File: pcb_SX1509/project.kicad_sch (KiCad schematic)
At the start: 43 parts, among them IC1 SX1509QBIULTRT

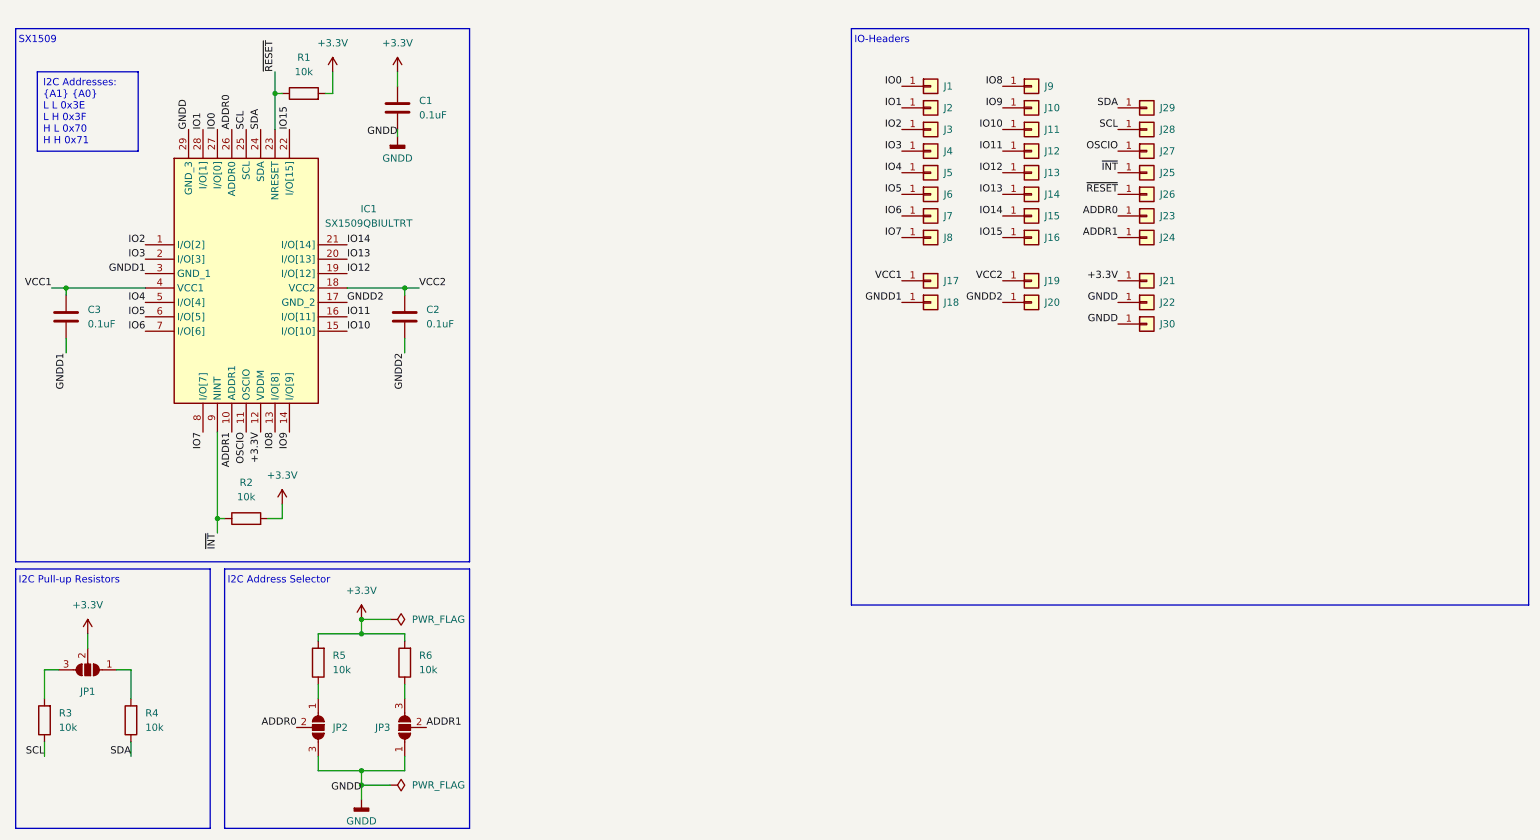
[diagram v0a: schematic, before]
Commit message: Standard output pin design for SX1509 PCB and add a new variant based on PCA9685
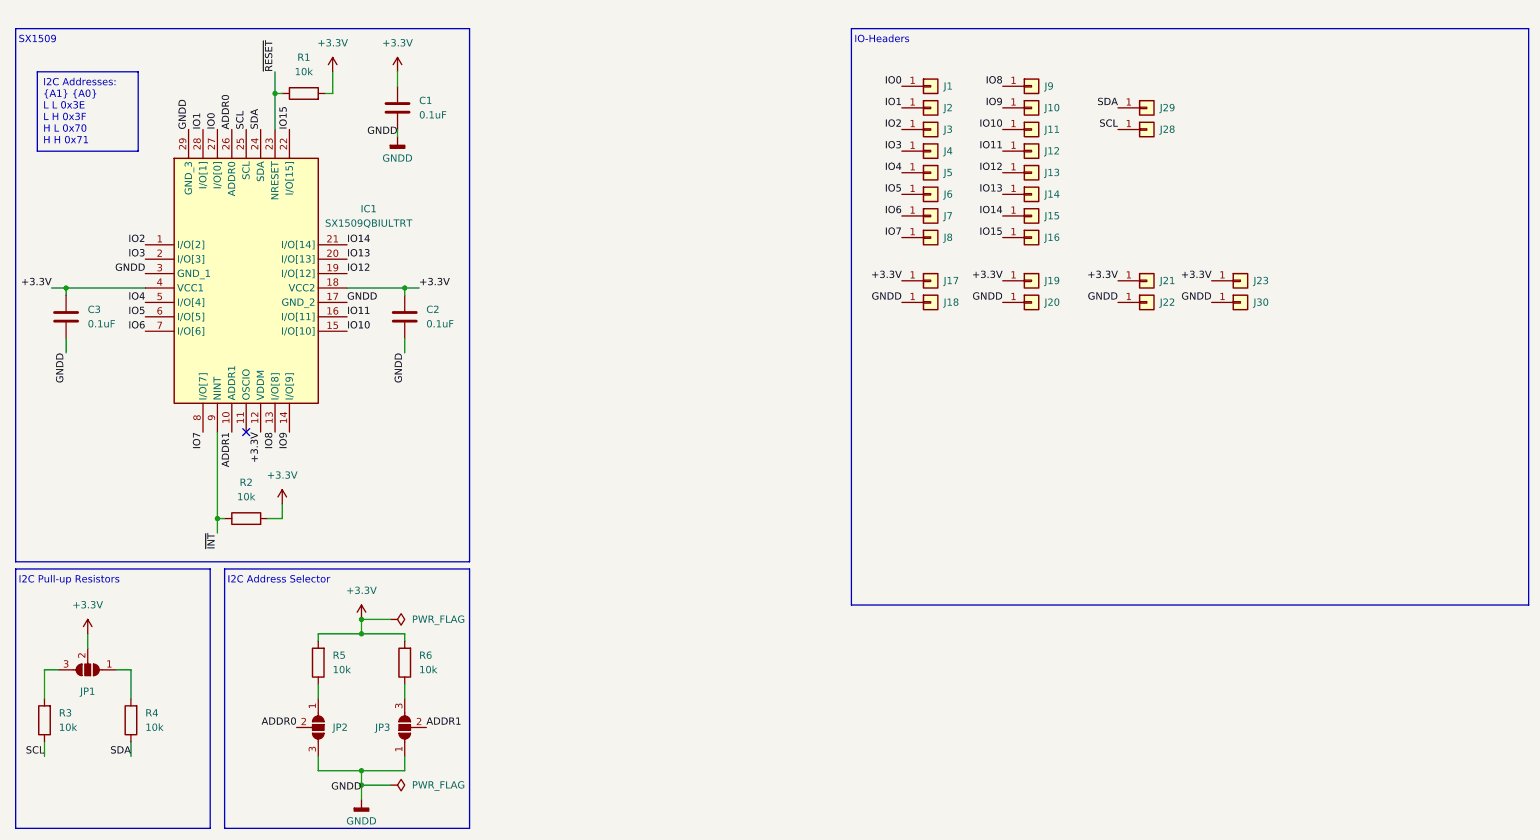
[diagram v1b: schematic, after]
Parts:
- removed J24, J25, J26, J27: ~, Castellated_Holes:Castellated_Hole02, symbol Connector_Generic:Conn_01x01
- JP1, JP2, JP3: footprint Jumper:SolderJumper-3_P1.3mm_Open_RoundedPad1.0x1.5mm -> Jumper:SolderJumper-3_P1.3mm_Open_RoundedPad1.0x1.5mm
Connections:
- net GNDD1 is gone; now on net GNDD: C3.2, IC1.3 (GND_1), J18.1 (Pin_1)
- net GNDD2 is gone; now on net GNDD: C2.2, IC1.17 (GND_2), J20.1 (Pin_1)
- net VCC1 is gone; now on net +3.3V: C3.1, IC1.4 (VCC1), J17.1 (Pin_1)
- net VCC2 is gone; now on net +3.3V: C2.1, IC1.18 (VCC2), J19.1 (Pin_1)
- net +3.3V: now also J23.1 (Pin_1)
- net ADDR0: no longer J23.1 (Pin_1)
- net OSCIO: no longer names the net of IC1.11 (OSCIO)
- no-connect marks 0 -> 1
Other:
- moved on the sheet: J30

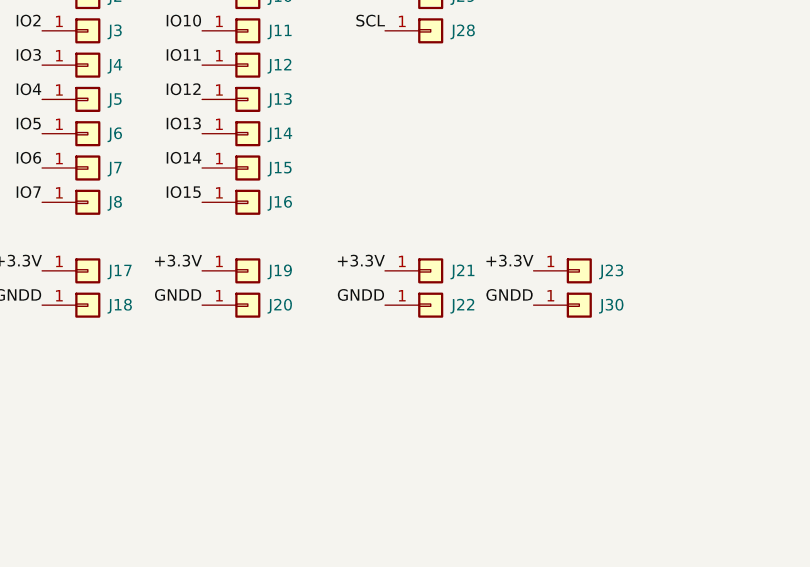
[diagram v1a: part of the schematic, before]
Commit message: Remove connector on own side
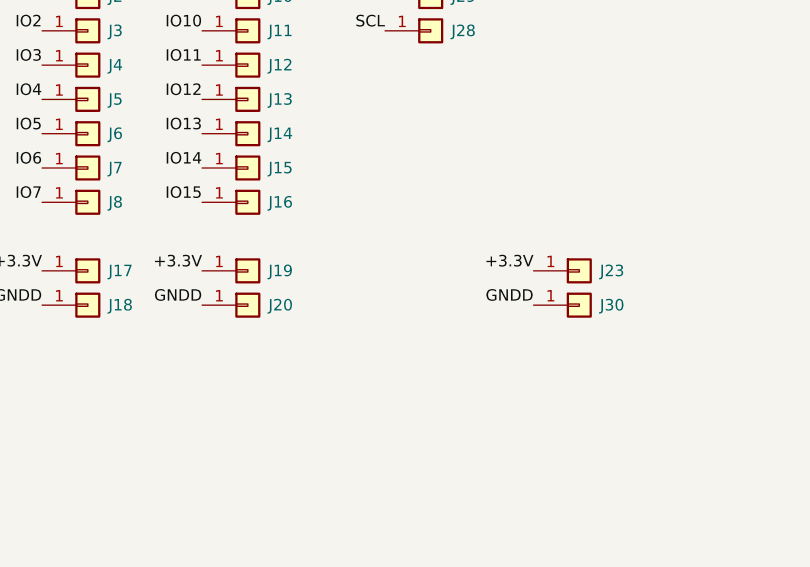
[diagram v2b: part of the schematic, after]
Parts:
- removed J21, J22: ~, Castellated_Holes:Castellated_Hole02, symbol Connector_Generic:Conn_01x01
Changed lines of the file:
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@@
-		)
-	)
-	(label "+3.3V"
-		(at 210.82 60.96 180)
-		(fields_autoplaced yes)
-		(effects
-			(font
-				(size 1.27 1.27)
-			)
-			(justify right bottom)
 		)
 	)
@@
 		)
 	)
-	(label "GNDD"
-		(at 210.82 64.77 180)
-		(fields_autoplaced yes)
-		(effects
-			(font
-				(size 1.27 1.27)
-			)
-			(justify right bottom)
-		)
-	)
 	(label "SCL"
 		(at 210.82 34.29 180)
@@
 	(symbol
 		(lib_id "Connector_Generic:Conn_01x01")
-		(at 215.9 60.96 0)
-		(unit 1)
-		(exclude_from_sim no)
-		(in_bom yes)
-		(on_board yes)
-		(dnp no)
-		(property "Reference" "J21"
-			(at 218.186 60.96 0)
-			(effects
-				(font
-					(size 1.27 1.27)
-				)
-				(justify left)
-			)
-		)
-		(property "Value" "~"
-			(at 218.44 62.2299 0)
-			(effects
-				(font
-					(size 1.27 1.27)
-				)
-				(justify left)
-			)
-		)
-		(property "Footprint" "Castellated_Holes:Castellated_Hole02"
-			(at 215.9 60.96 0)
-			(effects
-				(font
-					(size 1.27 1.27)
-				)
-				(hide yes)
-			)
-		)
-		(property "Datasheet" "~"
-			(at 215.9 60.96 0)
-			(effects
-				(font
-					(size 1.27 1.27)
-				)
-				(hide yes)
-			)
-		)
-		(property "Description" "Generic connector, single row, 01x01, script generated (kicad-library-utils/schlib/autogen/connector/)"
-			(at 215.9 60.96 0)
-			(effects
-				(font
-					(size 1.27 1.27)
-				)
-				(hide yes)
-			)
-		)
-		(pin "1"
-		)
-		(instances
-			(project "project"
-				(path "/eaded386-8ef5-4822-a552-66b037180f01"
-					(reference "J21")
-					(unit 1)
-				)
-			)
-		)
-	)
-	(symbol
-		(lib_id "Connector_Generic:Conn_01x01")
 		(at 177.8 26.67 0)
 		(unit 1)
@@
 					(unit 1)
 				)
-			)
-		)
-	)
-	(symbol
-		(lib_id "Connector_Generic:Conn_01x01")
-		(at 215.9 64.77 0)
-		(unit 1)
-		(exclude_from_sim no)
-		(in_bom yes)
-		(on_board yes)
-		(dnp no)
-		(property "Reference" "J22"
-			(at 218.186 64.77 0)
-			(effects
-				(font
-					(size 1.27 1.27)
-				)
-				(justify left)
-			)
-		)
-		(property "Value" "~"
-			(at 218.44 66.0399 0)
-			(effects
-				(font
-					(size 1.27 1.27)
-				)
-				(justify left)
-			)
-		)
-		(property "Footprint" "Castellated_Holes:Castellated_Hole02"
-			(at 215.9 64.77 0)
-			(effects
-				(font
-					(size 1.27 1.27)
-				)
-				(hide yes)
-			)
-		)
-		(property "Datasheet" "~"
-			(at 215.9 64.77 0)
-			(effects
-				(font
-					(size 1.27 1.27)
-				)
-				(hide yes)
-			)
-		)
-		(property "Description" "Generic connector, single row, 01x01, script generated (kicad-library-utils/schlib/autogen/connector/)"
-			(at 215.9 64.77 0)
-			(effects
-				(font
-					(size 1.27 1.27)
-				)
-				(hide yes)
-			)
-		)
-		(pin "1"
-		)
-		(instances
-			(project "project"
-				(path "/eaded386-8ef5-4822-a552-66b037180f01"
-					(reference "J22")
-					(unit 1)
-				)

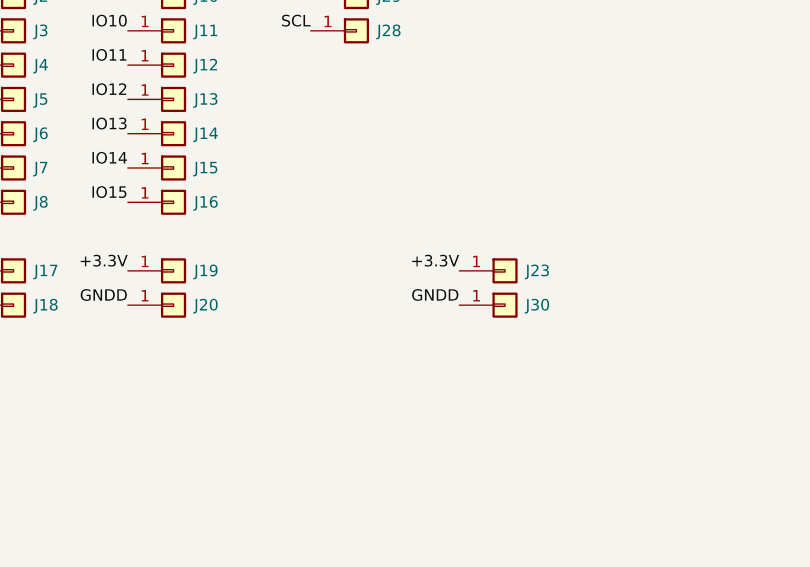
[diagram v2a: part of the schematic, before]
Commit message: Replace resistor array throw single resistor for reducing vias dn easy component selection
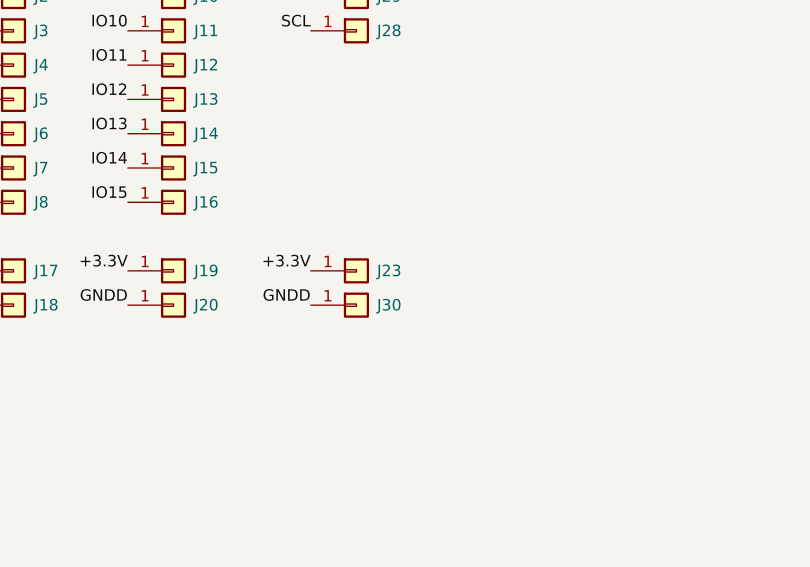
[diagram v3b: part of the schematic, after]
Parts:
- IC1: Mouser Price/Stock https://www.mouser.co.uk/ProductDetail/Semtech/SX1509QBIULT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 -> (none)
- J1, J10, J11, J12, J13, J14, J15, J16, J17, J18, J19, J2, J20, J23, J28, J29, J3, J30, J4, J5, J6, J7, J8, J9: now left out of the parts list
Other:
- moved on the sheet: J23, J30
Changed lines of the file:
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@@
 	)
 	(label "+3.3V"
-		(at 227.33 60.96 180)
+		(at 210.82 60.96 180)
 		(fields_autoplaced yes)
 		(effects
@@
 	)
 	(label "GNDD"
-		(at 227.33 64.77 180)
+		(at 210.82 64.77 180)
 		(fields_autoplaced yes)
 		(effects
@@
 			)
 		)
-		(property "Description" "Voltage Level Shifting GPIO with LED Driver 28-Pin QFN-UT EP T/R"
+		(property "Description" "SX1509QBIULTRT"
 			(at 39.37 54.61 0)
 			(effects
@@
 			)
 		)
-		(property "Mouser Price/Stock" "https://www.mouser.co.uk/ProductDetail/Semtech/SX1509QBIULTRT?qs=rBWM4%252BvDhIf3%2FilU3NIYqw%3D%3D"
-			(at 71.12 636.83 0)
-			(effects
-				(font
-					(size 1.27 1.27)
-				)
-				(justify left top)
-				(hide yes)
-			)
-		)
 		(property "Manufacturer_Name" "SEMTECH"
 			(at 71.12 736.83 0)
@@
 		(unit 1)
 		(exclude_from_sim no)
-		(in_bom yes)
+		(in_bom no)
 		(on_board yes)
 		(dnp no)
@@
 		(unit 1)
 		(exclude_from_sim no)
-		(in_bom yes)
+		(in_bom no)
 		(on_board yes)
 		(dnp no)
@@
 			)
 		)
-		(property "Description" "Resistor"
+		(property "Description" "Resistor, 10.0k, 0402 SMD"
 			(at 36.83 138.43 0)
 			(effects
@@
 		(unit 1)
 		(exclude_from_sim no)
-		(in_bom yes)
+		(in_bom no)
 		(on_board yes)
 		(dnp no)
@@
 		(unit 1)
 		(exclude_from_sim no)
-		(in_bom yes)
+		(in_bom no)
 		(on_board yes)
 		(dnp no)
@@
 		(unit 1)
 		(exclude_from_sim no)
-		(in_bom yes)
+		(in_bom no)
 		(on_board yes)
 		(dnp no)
@@
 		(unit 1)
 		(exclude_from_sim no)
-		(in_bom yes)
+		(in_bom no)
 		(on_board yes)
 		(dnp no)
@@
 		(unit 1)
 		(exclude_from_sim no)
-		(in_bom yes)
+		(in_bom no)
 		(on_board yes)
 		(dnp no)
@@
 			)
 		)
-		(property "Description" "Resistor"
+		(property "Description" "Resistor, 10.0k, 0402 SMD"
 			(at 69.85 128.27 0)
 			(effects
@@
 			)
 		)
-		(property "Description" "Unpolarized capacitor"
+		(property "Description" "Capacitor, 10uF, 0402 SMD"
 			(at 83.82 30.48 0)
 			(effects
@@
 			)
 		)
-		(property "Description" "Unpolarized capacitor"
+		(property "Description" "Capacitor, 10uF, 0402 SMD"
 			(at 25.4 67.31 0)
 			(effects
@@
 		(unit 1)
 		(exclude_from_sim no)
-		(in_bom yes)
+		(in_bom no)
 		(on_board yes)
 		(dnp no)
@@
 		(unit 1)
 		(exclude_from_sim no)
-		(in_bom yes)
+		(in_bom no)
 		(on_board yes)
 		(dnp no)
@@
 		(unit 1)
 		(exclude_from_sim no)
-		(in_bom yes)
+		(in_bom no)
 		(on_board yes)
 		(dnp no)
@@
 			)
 		)
-		(property "Description" "Resistor"
+		(property "Description" "Resistor, 10.0k, 0402 SMD"
 			(at 57.15 102.87 0)
 			(effects
@@
 		(unit 1)
 		(exclude_from_sim no)
-		(in_bom yes)
+		(in_bom no)
 		(on_board yes)
 		(dnp no)
@@
 		(unit 1)
 		(exclude_from_sim no)
-		(in_bom yes)
+		(in_bom no)
 		(on_board yes)
 		(dnp no)
@@
 		(unit 1)
 		(exclude_from_sim no)
-		(in_bom yes)
+		(in_bom no)
 		(on_board yes)
 		(dnp no)
@@
 		(unit 1)
 		(exclude_from_sim no)
-		(in_bom yes)
+		(in_bom no)
 		(on_board yes)
 		(dnp no)
@@
 			)
 		)
-		(property "Description" "Unpolarized capacitor"
+		(property "Description" "Capacitor, 10uF, 0402 SMD"
 			(at 85.09 67.31 0)
 			(effects
@@
 		(unit 1)
 		(exclude_from_sim no)
-		(in_bom yes)
+		(in_bom no)
 		(on_board yes)
 		(dnp no)
@@
 			)
 		)
-		(property "Description" "Resistor"
+		(property "Description" "Resistor, 10.0k, 0402 SMD"
 			(at 67.31 27.94 0)
 			(effects
@@
 	(symbol
 		(lib_id "Connector_Generic:Conn_01x01")
-		(at 232.41 64.77 0)
+		(at 215.9 64.77 0)
 		(unit 1)
 		(exclude_from_sim no)
-		(in_bom yes)
+		(in_bom no)
 		(on_board yes)
 		(dnp no)
 		(property "Reference" "J30"
-			(at 234.696 64.77 0)
+			(at 218.186 64.77 0)
 			(effects
 				(font
@@
 		)
 		(property "Value" "~"
-			(at 234.95 66.0399 0)
+			(at 218.44 66.0399 0)
 			(effects
 				(font
@@
 		)
 		(property "Footprint" "Castellated_Holes:Castellated_Hole02"
-			(at 232.41 64.77 0)
+			(at 215.9 64.77 0)
 			(effects
 				(font
@@
 		)
 		(property "Datasheet" "~"
-			(at 232.41 64.77 0)
+			(at 215.9 64.77 0)
 			(effects
 				(font
@@
 		)
 		(property "Description" "Generic connector, single row, 01x01, script generated (kicad-library-utils/schlib/autogen/connector/)"
-			(at 232.41 64.77 0)
+			(at 215.9 64.77 0)
 			(effects
 				(font
@@
 		(unit 1)
 		(exclude_from_sim no)
-		(in_bom yes)
+		(in_bom no)
 		(on_board yes)
 		(dnp no)
@@
 		(unit 1)
 		(exclude_from_sim no)
-		(in_bom yes)
+		(in_bom no)
 		(on_board yes)
 		(dnp no)
@@
 		(unit 1)
 		(exclude_from_sim no)
-		(in_bom yes)
+		(in_bom no)
 		(on_board yes)
 		(dnp no)
@@
 		(unit 1)
 		(exclude_from_sim no)
-		(in_bom yes)
+		(in_bom no)
 		(on_board yes)
 		(dnp no)
@@
 		(unit 1)
 		(exclude_from_sim no)
-		(in_bom yes)
+		(in_bom no)
 		(on_board yes)
 		(dnp no)
@@
 		(unit 1)
 		(exclude_from_sim no)
-		(in_bom yes)
+		(in_bom no)
 		(on_board yes)
 		(dnp no)
@@
 			)
 		)
-		(property "Description" "Resistor"
+		(property "Description" "Resistor, 10.0k, 0402 SMD"
 			(at 85.09 128.27 0)
 			(effects
@@
 	(symbol
 		(lib_id "Connector_Generic:Conn_01x01")
-		(at 232.41 60.96 0)
+		(at 215.9 60.96 0)
 		(unit 1)
 		(exclude_from_sim no)
-		(in_bom yes)
+		(in_bom no)
 		(on_board yes)
 		(dnp no)
 		(property "Reference" "J23"
-			(at 234.696 60.96 0)
+			(at 218.186 60.96 0)
 			(effects
 				(font
@@
 		)
 		(property "Value" "~"
-			(at 234.95 62.2299 0)
+			(at 218.44 62.2299 0)
 			(effects
 				(font
@@
 		)
 		(property "Footprint" "Castellated_Holes:Castellated_Hole02"
-			(at 232.41 60.96 0)
+			(at 215.9 60.96 0)
 			(effects
 				(font
@@
 		)
 		(property "Datasheet" "~"
-			(at 232.41 60.96 0)
+			(at 215.9 60.96 0)
 			(effects
 				(font
@@
 		)
 		(property "Description" "Generic connector, single row, 01x01, script generated (kicad-library-utils/schlib/autogen/connector/)"
-			(at 232.41 60.96 0)
+			(at 215.9 60.96 0)
 			(effects
 				(font
@@
 			)
 		)
-		(property "Description" "Resistor"
+		(property "Description" "Resistor, 10.0k, 0402 SMD"
 			(at 21.59 138.43 0)
 			(effects
@@
 		(unit 1)
 		(exclude_from_sim no)
-		(in_bom yes)
+		(in_bom no)
 		(on_board yes)
 		(dnp no)

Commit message: Correct some warnings and missing 3D step files
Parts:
- C1, C2, C3: AISLER_MPN (none) -> Capacitor, 10uF, 0402 SMD
- IC1: AISLER_MPN (none) -> SX1509QBIULTRT; LCSC# (none) -> C2652294
- R1, R2, R3, R4, R5, R6: AISLER_MPN (none) -> Resistor, 10.0k, 0402 SMD

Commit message: Add revision number to PCB
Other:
- company: (none) -> Thomas Fanninger
- title: (none) -> Breakout board: IO-Expander based on SX1509
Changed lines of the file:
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@@
 	(generator_version "8.0")
 	(paper "A4")
+	(title_block
+		(title "Breakout board: IO-Expander based on SX1509")
+		(date "2024-06-09")
+		(rev "1")
+		(company "Thomas Fanninger")
+	)
 	(junction
 		(at 25.4 62.23)
